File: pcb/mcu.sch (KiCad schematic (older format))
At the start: 23 parts, among them J1 Conn_01x04_Male, J2 Conn_01x03_Male, J3 Conn_01x03_Male, SW1 SW_Push, U1 STM32F103C8Tx, Y1 32.768KHz, Y2 8MHz

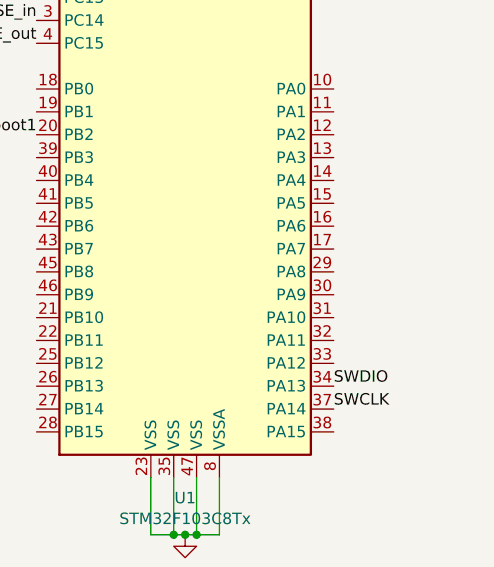
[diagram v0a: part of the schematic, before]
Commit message: [PCB & Firmware] Motors PWM Signal MCU Pins
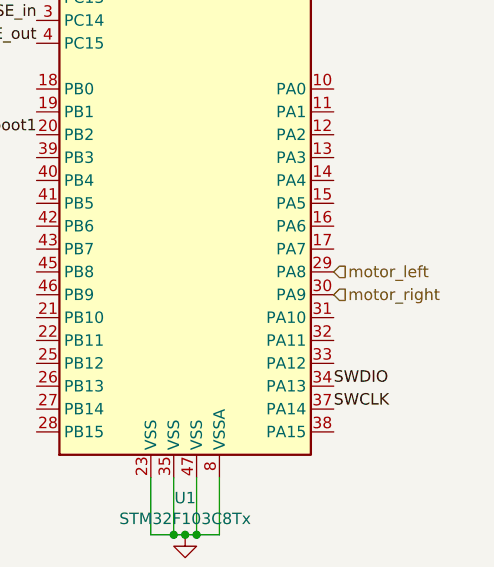
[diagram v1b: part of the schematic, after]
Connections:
- net motor_left: now reaches U1.29 (PA8)
- net motor_right: now reaches U1.30 (PA9)
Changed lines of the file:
@@
 Text Label 5050 3100 2    50   ~ 0
 LSE_out
+Text HLabel 6350 4100 2    50   Input ~ 0
+motor_left
+Text HLabel 6350 4200 2    50   Input ~ 0
+motor_right
 $EndSCHEMATC

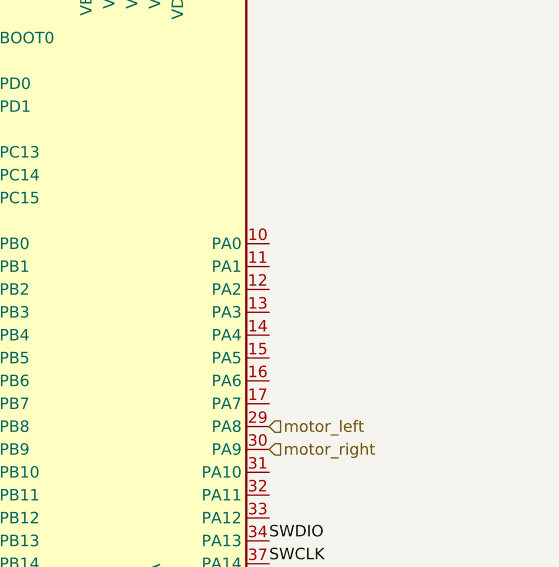
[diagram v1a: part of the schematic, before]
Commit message: [PCB & Firmware] Line Sensors MCU Pins
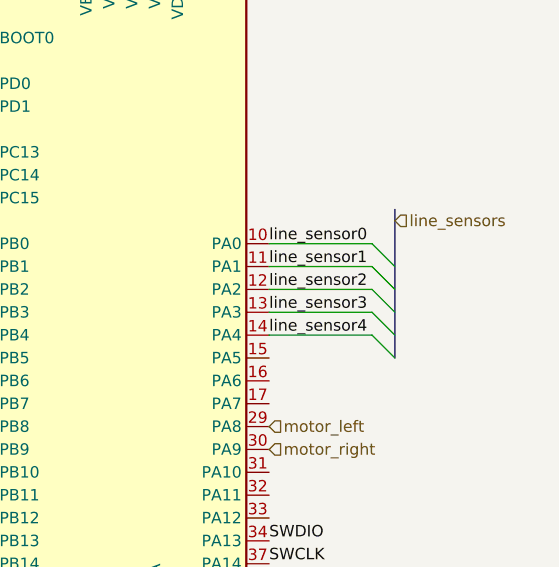
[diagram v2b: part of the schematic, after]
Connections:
- net line_sensor0: now reaches U1.10 (PA0)
- net line_sensor1: now reaches U1.11 (PA1)
- net line_sensor2: now reaches U1.12 (PA2)
- net line_sensor3: now reaches U1.13 (PA3)
- net line_sensor4: now reaches U1.14 (PA4)
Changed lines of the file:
@@
 Text HLabel 6350 4200 2    50   Input ~ 0
 motor_right
+Text Label 6350 3300 0    50   ~ 0
+line_sensor0
+Text Label 6350 3400 0    50   ~ 0
+line_sensor1
+Text Label 6350 3500 0    50   ~ 0
+line_sensor2
+Text Label 6350 3600 0    50   ~ 0
+line_sensor3
+Text Label 6350 3700 0    50   ~ 0
+line_sensor4
+Entry Wire Line
+	6800 3300 6900 3400
+Entry Wire Line
+	6800 3400 6900 3500
+Entry Wire Line
+	6800 3500 6900 3600
+Entry Wire Line
+	6800 3600 6900 3700
+Entry Wire Line
+	6800 3700 6900 3800
+Text HLabel 6900 3200 2    50   Input ~ 0
+line_sensors
+Wire Wire Line
+	6800 3300 6350 3300
+Wire Wire Line
+	6350 3400 6800 3400
+Wire Wire Line
+	6800 3500 6350 3500
+Wire Wire Line
+	6800 3600 6350 3600
+Wire Wire Line
+	6800 3700 6350 3700
+Wire Bus Line
+	6900 3150 6900 3800
 $EndSCHEMATC

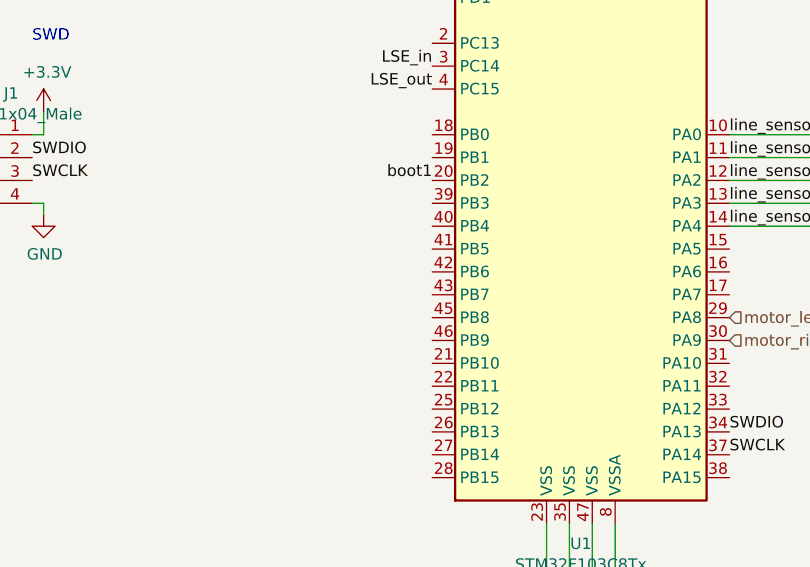
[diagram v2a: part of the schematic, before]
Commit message: [PCB & Firmware] I2C for LCD SSD1306 MCU Pins
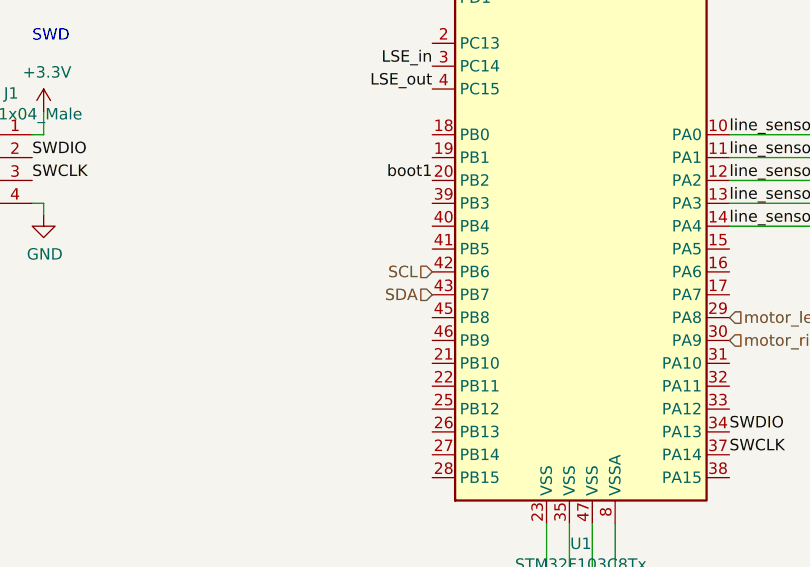
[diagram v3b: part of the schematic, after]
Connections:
- net SCL: now reaches U1.42 (PB6)
- net SDA: now reaches U1.43 (PB7)
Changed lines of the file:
@@
 Wire Bus Line
 	6900 3150 6900 3800
+Text HLabel 5050 3900 0    50   Input ~ 0
+SCL
+Text HLabel 5050 4000 0    50   Input ~ 0
+SDA
 $EndSCHEMATC

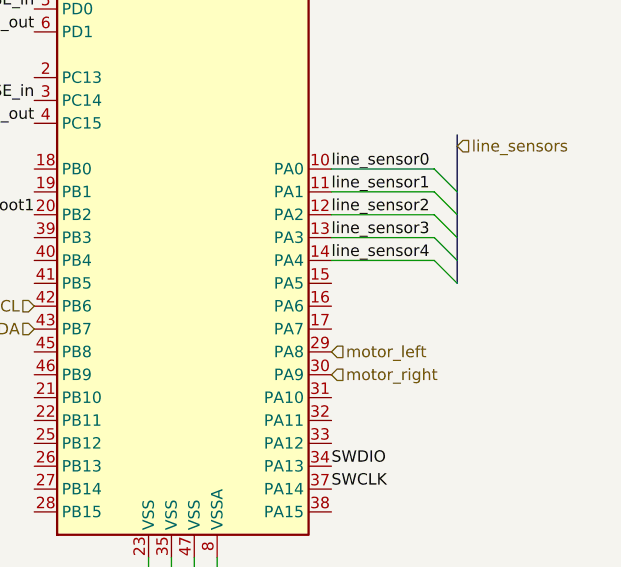
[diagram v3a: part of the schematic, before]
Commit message: [PCB & Firmware] Light Sensor MCU Pin
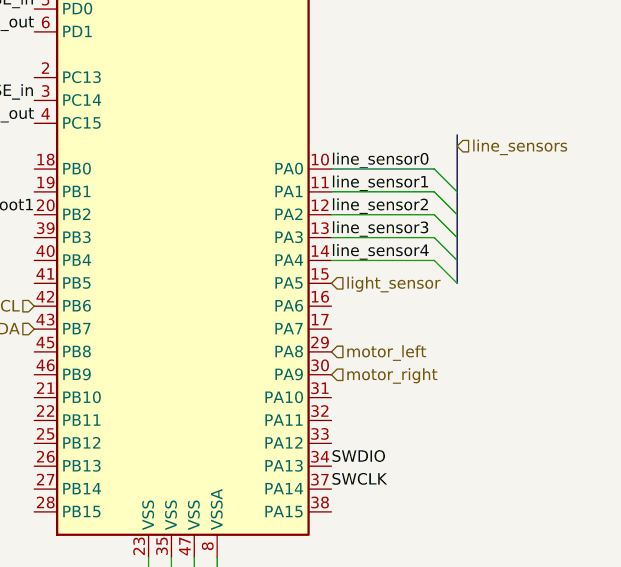
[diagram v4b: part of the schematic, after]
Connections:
- net light_sensor: now reaches U1.15 (PA5)
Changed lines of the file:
@@
 Text HLabel 5050 4000 0    50   Input ~ 0
 SDA
+Text HLabel 6350 3800 2    50   Input ~ 0
+light_sensor
 $EndSCHEMATC

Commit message: IR matrix
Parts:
- added J2: Conn_01x04_Male, Connector_PinHeader_2.54mm:PinHeader_1x04_P2.54mm_Vertical, symbol Connector:Conn_01x04_Male
- renumbered C11 to C10, C9 to C11, C10 to C9, J2 to J3, J3 to J4, R3 to R1, R1 to R2, R2 to R3
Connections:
- net +3V3: now also J2.1 (Pin_1)
- net GND: now also J2.4 (Pin_4)
- net SWCLK: no longer U1.37 (PA14)
- net SWDIO: no longer U1.34 (PA13)
- net SCL renamed TX
- net TX: now also J2.2 (Pin_2)
- net SDA renamed RX
- net RX: now also J2.3 (Pin_3)
- net light_sensor: no longer names the net of U1.15 (PA5)
- net line_sensor0: no longer names the net of U1.10 (PA0)
- net line_sensor1: no longer names the net of U1.11 (PA1)
- net line_sensor2: no longer names the net of U1.12 (PA2)
- net line_sensor3: no longer names the net of U1.13 (PA3)
- net line_sensor4: no longer names the net of U1.14 (PA4)
- net motor_left: no longer names the net of U1.29 (PA8)
- net motor_right: no longer names the net of U1.30 (PA9)
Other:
- note added: "Programming"
- note added: "Programming Serial"
- note added: "TODO: Connct to MCU"
- moved on the sheet: C11, D1, J1, J3, J4, R1, R2, R3, R4, SW1, U1
